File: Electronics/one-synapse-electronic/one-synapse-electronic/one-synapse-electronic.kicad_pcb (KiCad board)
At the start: 2 copper layers, 127 parts, among them J1 prg-err, J2 Axon, J3 Axon, J4 PWM-in, J5 PWM-out, J6 pwr, J7 synapses, Q17 BS170F, Q18 BS170F, Q19 BS170F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

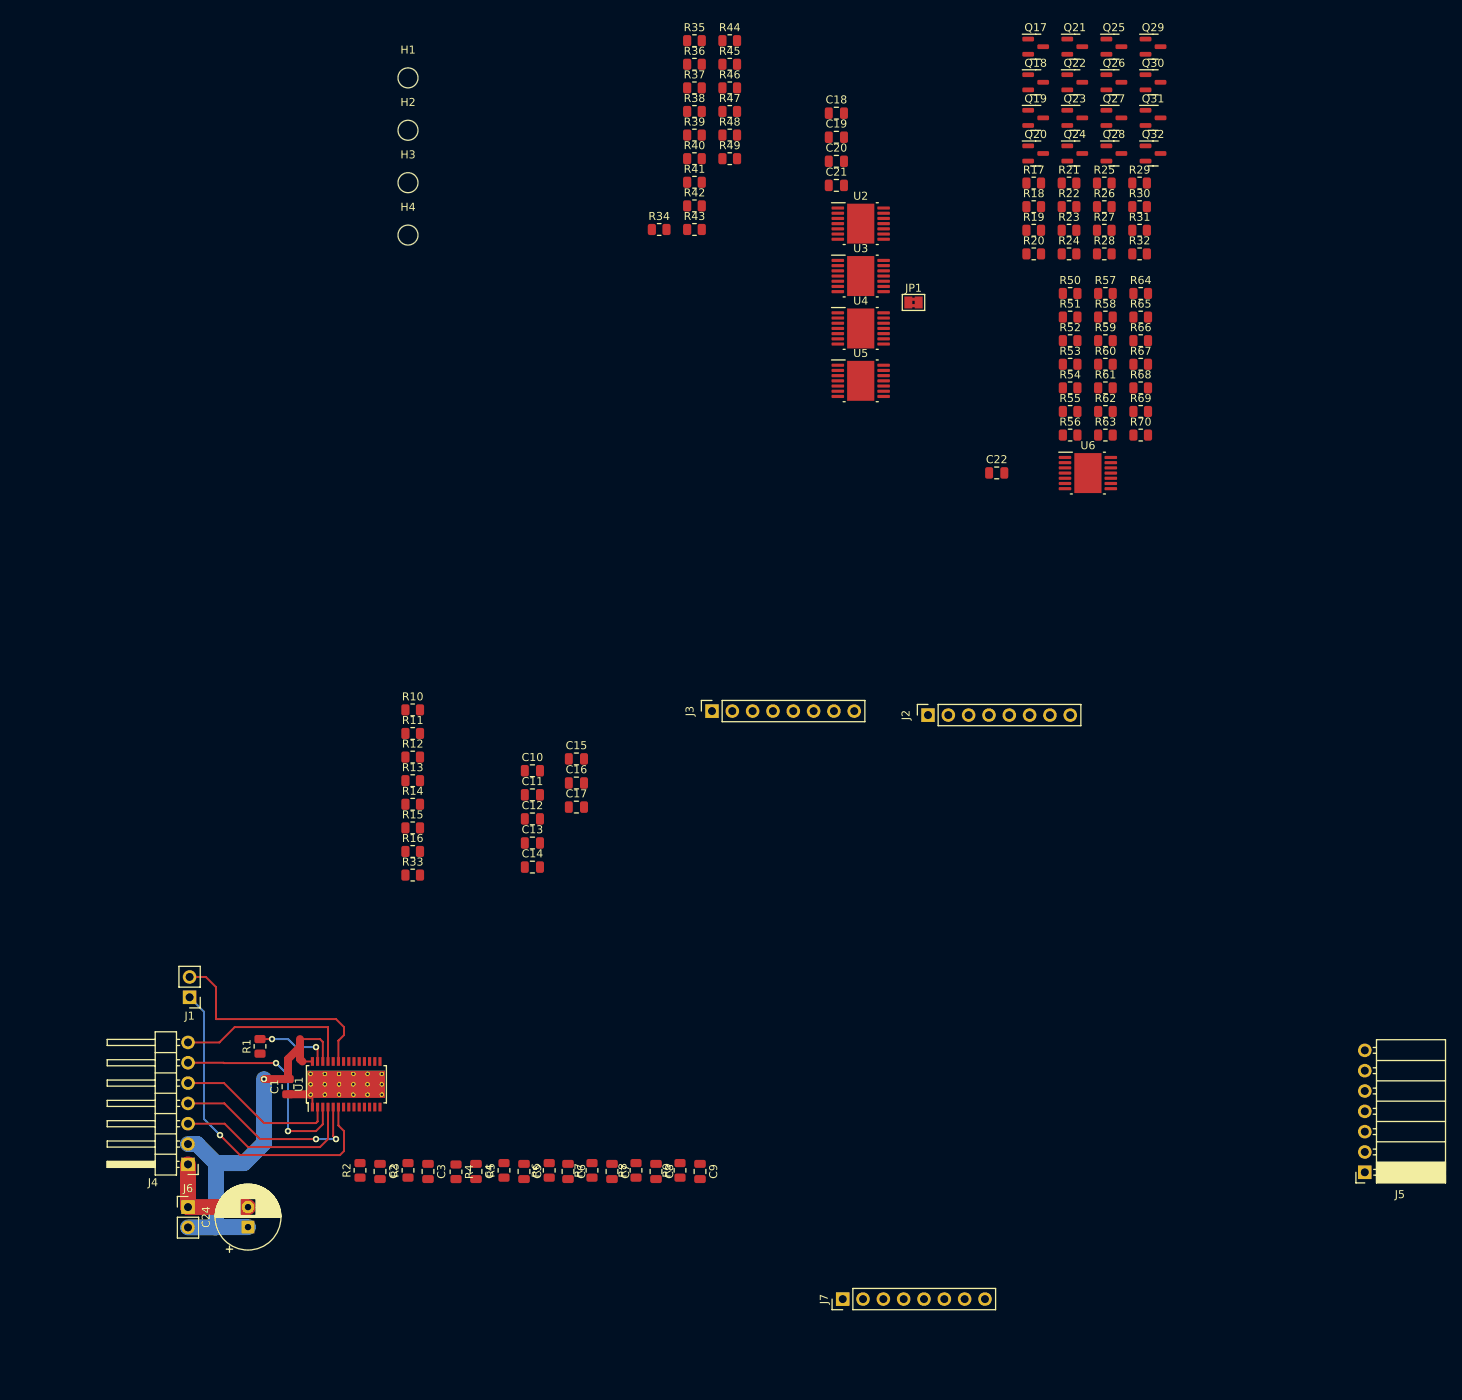
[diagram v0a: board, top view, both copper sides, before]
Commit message: WIP. Added combiner i/o.
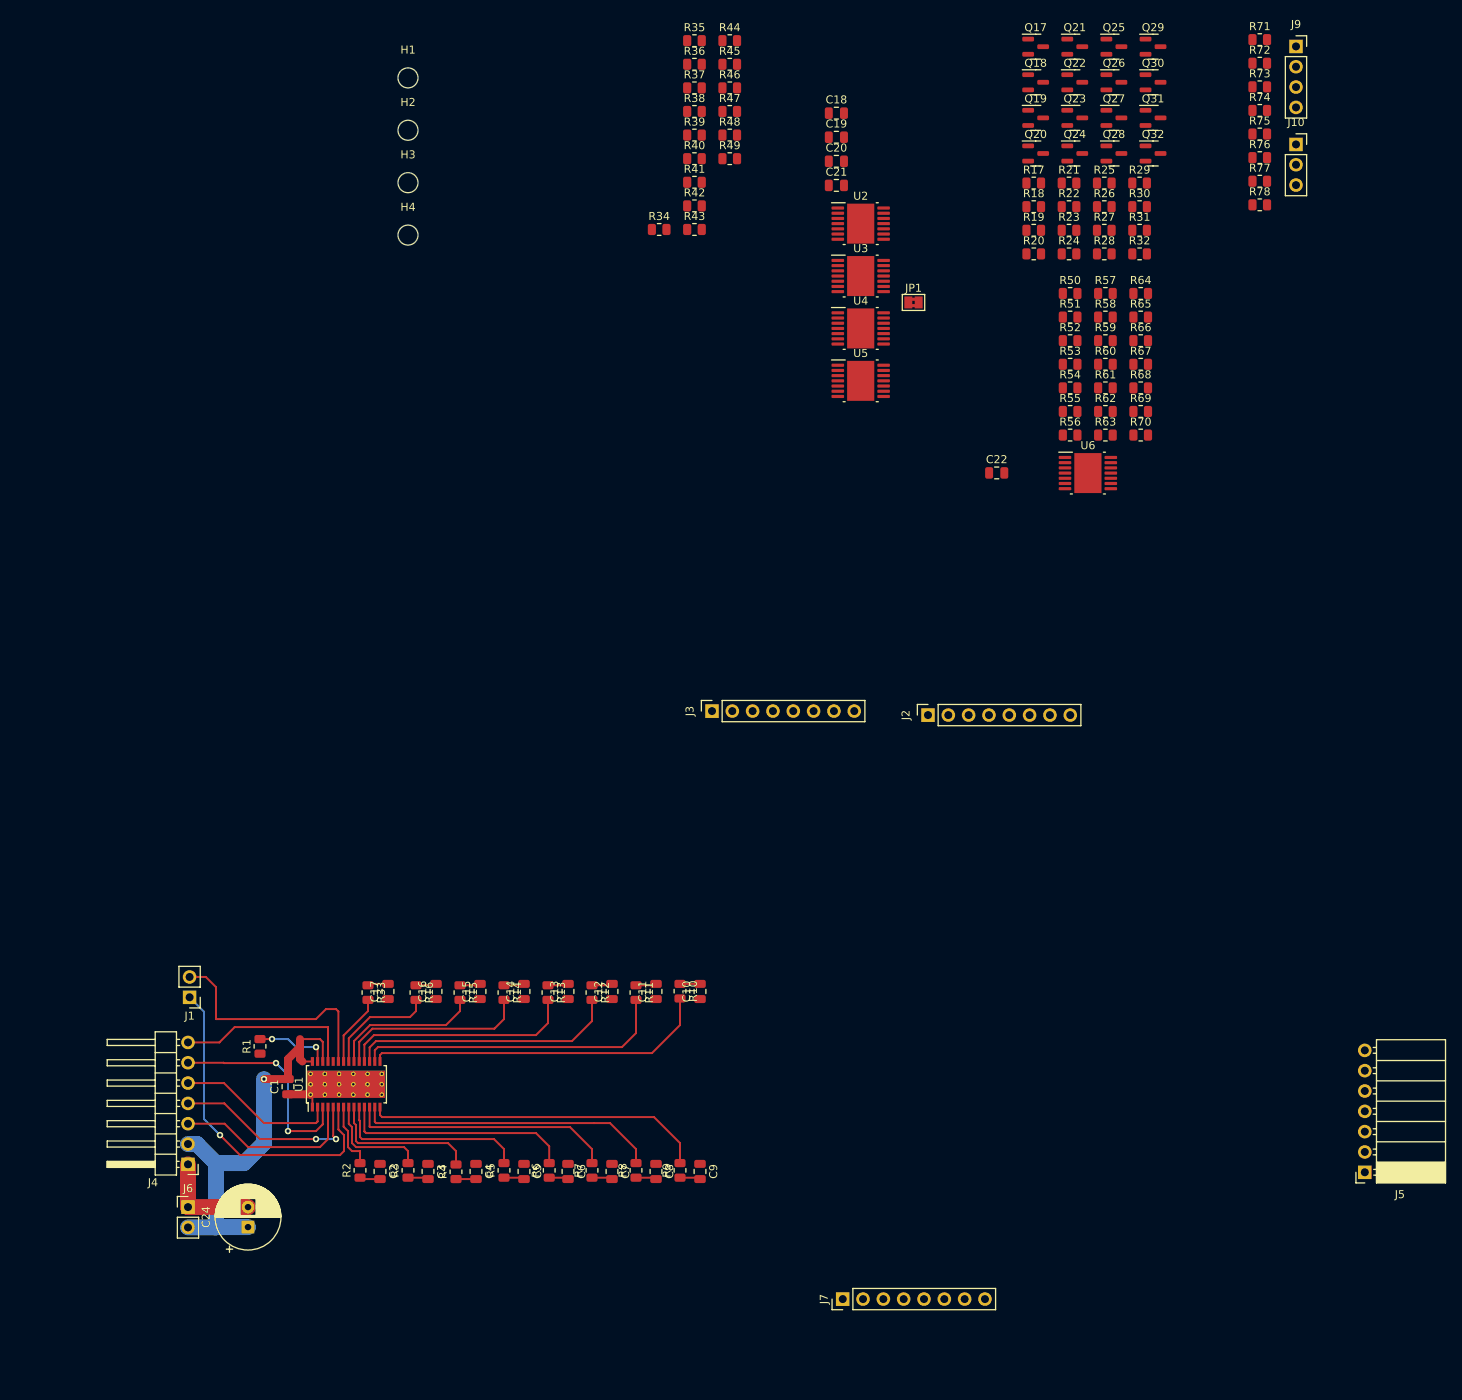
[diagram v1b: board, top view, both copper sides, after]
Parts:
- added J10: comb, Connector_PinSocket_2.54mm:PinSocket_1x03_P2.54mm_Vertical, F.Cu at (193.0, 31.7)
- added J9: sel, Connector_PinSocket_2.54mm:PinSocket_1x04_P2.54mm_Vertical, F.Cu at (193.0, 19.4)
- added R71: 22K, Resistor_SMD:R_0805_2012Metric, F.Cu at (188.5, 18.6)
- added R72: 22K, Resistor_SMD:R_0805_2012Metric, F.Cu at (188.5, 21.5)
- added R73: 22K, Resistor_SMD:R_0805_2012Metric, F.Cu at (188.5, 24.5)
- added R74: 22K, Resistor_SMD:R_0805_2012Metric, F.Cu at (188.5, 27.4)
- added R75: 22K, Resistor_SMD:R_0805_2012Metric, F.Cu at (188.5, 30.4)
- added R76: 22K, Resistor_SMD:R_0805_2012Metric, F.Cu at (188.5, 33.3)
- added R77: 22K, Resistor_SMD:R_0805_2012Metric, F.Cu at (188.5, 36.3)
- added R78: 22K, Resistor_SMD:R_0805_2012Metric, F.Cu at (188.5, 39.2)
- moved R10 48.5 mm to (116.0, 137.5), turned to -90 degrees
- moved R11 42.8 mm to (110.5, 137.7), turned to -90 degrees
- moved R12 37.0 mm to (105.0, 137.7), turned to -90 degrees
- moved C10 34.6 mm to (118.5, 137.6), turned to 90 degrees
- moved C17 33.0 mm to (79.5, 137.6), turned to 90 degrees
- moved C15 31.5 mm to (91.0, 137.6), turned to 90 degrees
- moved R13 31.4 mm to (99.5, 137.7), turned to -90 degrees
- moved C16 31.4 mm to (85.5, 137.6), turned to 90 degrees
- moved C11 29.0 mm to (113.0, 137.6), turned to 90 degrees
- moved R14 26.2 mm to (94.0, 137.7), turned to -90 degrees
- moved C12 23.8 mm to (107.5, 137.6), turned to 90 degrees
- moved R15 21.4 mm to (88.5, 137.7), turned to -90 degrees
- moved C13 19.1 mm to (102.0, 137.6), turned to 90 degrees
- moved R16 17.6 mm to (83.0, 137.7), turned to -90 degrees
- moved R33 15.7 mm to (77.0, 137.7), turned to -90 degrees
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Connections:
- R50 pad 1: Net-(U6B-+) -> Net-(J9-Pin_4)
- U6 pad 1: Net-(U6B-+) -> Net-(J9-Pin_4)
- U6 pad 10: unconnected-(U6C-+-Pad10) -> Net-(U6C-+)
- U6 pad 12: unconnected-(U6D-+-Pad12) -> Net-(U6D-+)
- U6 pad 13: unconnected-(U6D---Pad13) -> Net-(U6D--)
- U6 pad 14: unconnected-(U6-Pad14) -> Net-(J9-Pin_2)
- U6 pad 5: Net-(U6B-+) -> Net-(J9-Pin_3)
- U6 pad 8: unconnected-(U6-Pad8) -> Net-(J9-Pin_1)
- U6 pad 9: unconnected-(U6C---Pad9) -> Net-(U6C--)
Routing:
- net Net-(U1-OUT8): track 0.00 -> 43.2 mm
- net Net-(U1-OUT7): track 0.00 -> 42.4 mm
- net Net-(U1-OUT9): track 0.00 -> 39.1 mm
- net Net-(U1-OUT6): track 0.00 -> 37.7 mm
- net Net-(U1-OUT10): track 0.00 -> 33.6 mm
- net Net-(U1-OUT5): track 0.00 -> 33.2 mm
- net Net-(U1-OUT11): track 0.00 -> 29.1 mm
- net Net-(U1-OUT4): track 0.00 -> 29.0 mm
- net Net-(U1-OUT3): track 0.00 -> 24.2 mm
- net Net-(U1-OUT12): track 0.00 -> 24.1 mm
- net Net-(U1-OUT2): track 0.00 -> 19.0 mm
- net Net-(U1-OUT13): track 0.00 -> 18.8 mm
- net Net-(U1-OUT14): track 0.00 -> 14.1 mm
- net Net-(U1-OUT1): track 0.00 -> 13.6 mm
- net Net-(U1-OUT15): track 0.00 -> 8.96 mm
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
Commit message: PCB WIP
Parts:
- moved U2 143.2 mm to (80.0, 172.3)
- moved U3 125.9 mm to (95.0, 166.3)
- moved R37 116.7 mm to (117.3, 141.3)
- moved R42 116.7 mm to (117.3, 156.1)
- moved R46 116.7 mm to (121.7, 141.3)
- moved R34 116.7 mm to (112.9, 159.0)
- moved R35 116.7 mm to (117.3, 135.4)
- moved R38 116.7 mm to (117.3, 144.2)
- moved R40 116.7 mm to (117.3, 150.2)
- moved R43 116.7 mm to (117.3, 159.0)
- moved R44 116.7 mm to (121.7, 135.4)
- moved R47 116.7 mm to (121.7, 144.2)
- moved R49 116.7 mm to (121.7, 150.2)
- moved R36 116.7 mm to (117.3, 138.3)
- moved R39 116.7 mm to (117.3, 147.2)
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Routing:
- net Net-(U1-OUT8): track 43.2 -> 14.6 mm
- net Net-(U1-OUT7): track 42.4 -> 15.2 mm
- net Net-(U1-OUT9): track 39.1 -> 13.2 mm
- net Net-(U1-OUT6): track 37.7 -> 14.1 mm
- net Net-(U1-OUT10): track 33.6 -> 11.8 mm
- net Net-(U1-OUT5): track 33.2 -> 12.7 mm
- net Net-(U1-OUT11): track 29.1 -> 10.4 mm
- net Net-(U1-OUT4): track 29.0 -> 11.0 mm
- net Net-(U1-OUT12): track 24.1 -> 9.40 mm
- net Net-(U1-OUT3): track 24.2 -> 9.99 mm
- net Net-(U1-OUT13): track 18.8 -> 7.98 mm
- net Net-(U1-OUT2): track 19.0 -> 8.86 mm
- net Net-(U1-OUT14): track 14.1 -> 8.38 mm
- net Sout: track 0.00 -> 5.47 mm, vias 0 -> 1
- net Net-(U1-OUT1): track 13.6 -> 8.58 mm
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
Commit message: PCB WIP
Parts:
- moved R36 65.3 mm to (64.5, 176.8), turned to 90 degrees
- moved R35 64.6 mm to (64.2, 172.2), turned to 90 degrees
- moved R49 62.6 mm to (64.2, 125.5), turned to 90 degrees
- moved R46 58.4 mm to (64.2, 131.0), turned to 90 degrees
- moved R37 56.2 mm to (72.5, 175.2), turned to -90 degrees
- moved R48 53.6 mm to (72.8, 125.5), turned to 90 degrees
- moved R47 50.8 mm to (72.8, 131.0), turned to 90 degrees
- moved R40 43.8 mm to (82.8, 177.0), turned to 90 degrees
- moved R42 43.8 mm to (82.8, 129.2), turned to -90 degrees
- moved R45 42.3 mm to (81.8, 124.5)
- moved R39 42.0 mm to (82.8, 171.0), turned to 90 degrees
- moved R34 41.7 mm to (72.5, 169.2), turned to -90 degrees
- moved R43 38.3 mm to (91.0, 131.2), turned to 90 degrees
- moved R38 36.3 mm to (91.0, 169.2), turned to -90 degrees
- moved R41 34.3 mm to (91.0, 175.0), turned to -90 degrees
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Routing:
- net Vcc: track 52.3 -> 155.6 mm, vias 1 -> 5
- net PB6: track 1.80 -> 34.7 mm, vias 1 -> 2
- net PB3: track 1.89 -> 34.5 mm, vias 1 -> 2
- net PC2: track 1.89 -> 31.6 mm, vias 1 -> 2
- net PB2: track 1.89 -> 30.8 mm, vias 1 -> 2
- net PB7: track 2.09 -> 30.6 mm, vias 1 -> 2
- net PC7: track 2.37 -> 29.2 mm, vias 1 -> 2
- net PC3: track 1.89 -> 25.3 mm, vias 1 -> 2
- net PC6: track 2.11 -> 25.0 mm, vias 1 -> 0
- net PC4: track 1.89 -> 23.1 mm, vias 1 -> 2
- net PC0: track 2.14 -> 20.2 mm, vias 1 -> 2
- net PC5: track 1.89 -> 17.6 mm, vias 1 -> 2
- net PB1: track 2.15 -> 17.0 mm, vias 1 -> 2
- net PB5: track 1.89 -> 16.5 mm, vias 1 -> 2
- net PB4: track 2.14 -> 16.1 mm, vias 1 -> 2
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
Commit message: PCB WIP
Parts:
- moved C20 147.5 mm to (67.8, 164.8), turned to -90 degrees
- moved C21 141.0 mm to (82.8, 167.5)
- moved H1 128.9 mm to (34.2, 143.1)
- moved H2 128.9 mm to (34.2, 149.7)
- moved H3 128.9 mm to (34.2, 156.2)
- moved H4 128.9 mm to (34.2, 162.8)
- moved C18 128.4 mm to (63.8, 134.2)
- moved C19 115.3 mm to (82.8, 133.2), turned to -90 degrees
- moved R71 105.2 mm to (156.5, 118.8)
- moved R72 105.2 mm to (156.5, 121.7)
- moved R73 105.2 mm to (156.5, 124.7)
- moved R75 105.2 mm to (156.5, 130.6)
- moved R76 105.2 mm to (156.5, 133.5)
- moved R78 105.2 mm to (156.5, 139.4)
- moved R74 105.2 mm to (156.5, 127.6)
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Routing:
- net B1: track 0.00 -> 70.9 mm
- net C7: track 0.00 -> 65.8 mm
- net B0: track 0.00 -> 63.2 mm, vias 0 -> 1
- net B2: track 0.00 -> 62.1 mm
- net B3: track 0.00 -> 54.4 mm, vias 0 -> 1
- net B7: track 0.00 -> 53.6 mm, vias 0 -> 2
- net B5: track 0.00 -> 52.2 mm
- net C4: track 0.00 -> 50.2 mm, vias 0 -> 2
- net B6: track 0.00 -> 42.2 mm
- net B4: track 0.00 -> 41.1 mm, vias 0 -> 1
- net C5: track 0.00 -> 35.2 mm, vias 0 -> 1
- net C0: track 0.00 -> 30.8 mm, vias 0 -> 1
- net C6: track 0.00 -> 30.5 mm, vias 0 -> 1
- net C3: track 0.00 -> 18.9 mm
- net C1: track 0.00 -> 18.0 mm, vias 0 -> 1
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
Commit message: PCB WIP
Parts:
- moved R57 76.8 mm to (107.0, 141.2), turned to -90 degrees
- moved R65 76.6 mm to (107.0, 146.0), turned to -90 degrees
- moved R64 72.8 mm to (107.0, 157.2), turned to -90 degrees
- moved R66 71.0 mm to (107.0, 134.2), turned to -90 degrees
- moved R58 66.9 mm to (107.0, 130.0), turned to -90 degrees
- moved R63 66.9 mm to (107.2, 168.5), turned to -90 degrees
- moved R52 62.9 mm to (121.2, 147.2), turned to 90 degrees
- moved R55 62.3 mm to (107.2, 164.2), turned to -90 degrees
- moved R56 61.6 mm to (107.0, 153.0), turned to -90 degrees
- moved R61 53.1 mm to (123.6, 130.5), turned to 90 degrees
- moved R60 52.0 mm to (121.2, 142.7), turned to 90 degrees
- moved R59 49.7 mm to (124.0, 153.2), turned to -90 degrees
- moved R62 48.0 mm to (126.5, 140.9), turned to -90 degrees
- moved R53 46.6 mm to (123.6, 134.7), turned to 90 degrees
- moved R51 45.2 mm to (124.0, 148.9), turned to -90 degrees
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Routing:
- net Net-(U6A-+): track 0.00 -> 92.1 mm
- net B7: track 53.6 -> 33.6 mm, vias 2 -> 1
- net Net-(U6A--): track 0.00 -> 19.2 mm
- net C7: track 65.8 -> 49.8 mm
- net B6: track 42.2 -> 45.9 mm
- net C6: track 30.5 -> 34.1 mm
- net C5: track 35.2 -> 38.8 mm
- net B5: track 52.2 -> 55.8 mm
- net C1: track 18.0 -> 21.3 mm
- net C2: track 14.1 -> 17.4 mm
- net B2: track 62.1 -> 65.4 mm
- net C3: track 18.9 -> 22.2 mm
- net B3: track 54.4 -> 57.7 mm
- net C4: track 50.2 -> 53.5 mm
- net B4: track 41.1 -> 44.4 mm
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
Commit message: PCB WIP
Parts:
- moved H2 105.9 mm to (137.8, 127.2)
- moved H3 105.3 mm to (138.8, 168.8)
- moved J5 60.8 mm to (140.8, 159.2)
- moved J2 50.1 mm to (98.8, 116.8)
- moved H1 32.1 mm to (55.8, 119.2)
- moved R66 30.9 mm to (112.0, 164.8), turned to 90 degrees
- moved R77 29.9 mm to (127.1, 142.1)
- moved R71 29.9 mm to (127.1, 124.3)
- moved R72 29.9 mm to (127.1, 127.3)
- moved R73 29.9 mm to (127.1, 130.2)
- moved R74 29.9 mm to (127.1, 133.2)
- moved R75 29.9 mm to (127.1, 136.2)
- moved R76 29.9 mm to (127.1, 139.1)
- moved R78 29.9 mm to (127.1, 145.0)
- moved Q30 29.1 mm to (115.0, 162.9)
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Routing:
- net Net-(U6A--): track 19.2 -> 132.0 mm, vias 0 -> 2
- net S2: track 7.70 -> 109.3 mm, vias 0 -> 4
- net C4: track 53.5 -> 140.4 mm
- net S1: track 8.15 -> 82.2 mm, vias 0 -> 2
- net S6: track 7.55 -> 78.6 mm, vias 0 -> 4
- net C7: track 49.8 -> 116.2 mm, vias 0 -> 2
- net C5: track 38.8 -> 105.2 mm, vias 1 -> 2
- net Net-(U6A-+): track 92.1 -> 155.5 mm, vias 0 -> 2
- net S3: track 7.38 -> 62.5 mm, vias 0 -> 2
- net C6: track 34.1 -> 88.1 mm, vias 1 -> 2
- net S5: track 7.55 -> 52.0 mm, vias 0 -> 4
- net S0: track 8.09 -> 49.4 mm, vias 0 -> 2
- net S7: track 7.34 -> 41.4 mm, vias 0 -> 2
- net B2: track 65.4 -> 98.7 mm
- net B3: track 57.7 -> 89.4 mm, vias 1 -> 2
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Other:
- board outline added: 91.8 x 71 mm

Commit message: PCB WIP
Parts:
- moved J9 68.0 mm to (128.4, 143.2), turned to 90 degrees
- moved JP1 65.0 mm to (66.8, 160.5), turned to -90 degrees
- moved J10 61.6 mm to (130.9, 145.8), turned to 90 degrees
- moved R20 54.1 mm to (130.0, 124.5)
- moved J7 54.1 mm to (140.1, 128.4)
- moved R72 48.9 mm to (126.6, 176.2), turned to -90 degrees
- moved R71 47.5 mm to (124.4, 171.8), turned to -90 degrees
- moved R74 47.0 mm to (129.2, 180.2)
- moved R21 46.1 mm to (132.6, 132.4), turned to -90 degrees
- moved R22 46.1 mm to (135.1, 132.4), turned to -90 degrees
- moved R23 46.1 mm to (137.6, 132.4), turned to -90 degrees
- moved R24 46.1 mm to (140.1, 132.4), turned to -90 degrees
- moved R19 46.0 mm to (127.5, 132.5), turned to -90 degrees
- moved R17 46.0 mm to (122.2, 132.5), turned to -90 degrees
- moved R18 46.0 mm to (124.8, 132.5), turned to -90 degrees
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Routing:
- net Sout: track 5.47 -> 171.6 mm, vias 1 -> 2
- net Vcc: track 159.4 -> 309.5 mm, vias 6 -> 8
- net GSCLK: track 22.6 -> 172.0 mm
- net SCLK: track 23.1 -> 167.5 mm
- net BLANK: track 20.2 -> 163.5 mm, vias 0 -> 1
- net XLAT: track 27.0 -> 167.5 mm, vias 2 -> 3
- net S3: track 62.5 -> 24.1 mm
- net S5: track 52.0 -> 90.1 mm
- net S6: track 78.6 -> 116.5 mm, vias 4 -> 2
- net S2: track 109.3 -> 145.6 mm, vias 4 -> 6
- net S1: track 82.2 -> 117.8 mm
- net S4: track 28.3 -> 60.0 mm
- net S0: track 49.4 -> 23.9 mm
- net Net-(U6C-+): track 0.00 -> 25.1 mm, vias 0 -> 3
- net S7: track 41.4 -> 63.3 mm
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- added copper zone on B.Cu, net GND
- added copper zone on F.Cu, net GND
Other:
- board size 91.8 x 71 mm -> 92.2 x 72.5 mm

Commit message: The first(!) final PCB design...
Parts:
- moved R68 1.46 mm to (132.6, 151.2), turned to 180 degrees
- moved R50 1.36 mm to (132.4, 158.6)
- moved R67 0.20 mm to (134.4, 153.8)
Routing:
- net Net-(J2-Pin_1): track 0.00 -> 110.3 mm, vias 0 -> 1
- net Net-(J9-Pin_2): track 4.33 -> 62.5 mm, vias 0 -> 2
- net Net-(J10-Pin_2): track 3.80 -> 54.5 mm, vias 0 -> 1
- net Net-(J9-Pin_1): track 3.29 -> 40.6 mm, vias 0 -> 1
- net Net-(J9-Pin_3): track 0.00 -> 37.2 mm, vias 0 -> 3
- net Net-(J9-Pin_4): track 7.89 -> 28.6 mm, vias 0 -> 1
- net Net-(J10-Pin_3): track 2.80 -> 21.6 mm, vias 0 -> 1
- net Net-(U6D-+): track 20.7 -> 32.9 mm
- net GND: track 44.8 -> 46.5 mm, vias 31 -> 37
- net Net-(U6A-+): track 169.3 -> 168.3 mm
- net S2: track 145.6 -> 146.5 mm
- net Sout: track 171.6 -> 170.8 mm
- net Net-(U6B--): track 6.71 -> 7.51 mm
- net GSCLK: track 172.0 -> 171.4 mm
- net Vcc: track 309.5 -> 309.8 mm, vias 8 -> 9
